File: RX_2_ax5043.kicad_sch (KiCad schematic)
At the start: 19 parts, among them P2 CONUFL001-SMD-T, Q4 DMP2160UWQ-7, U15 AX5043

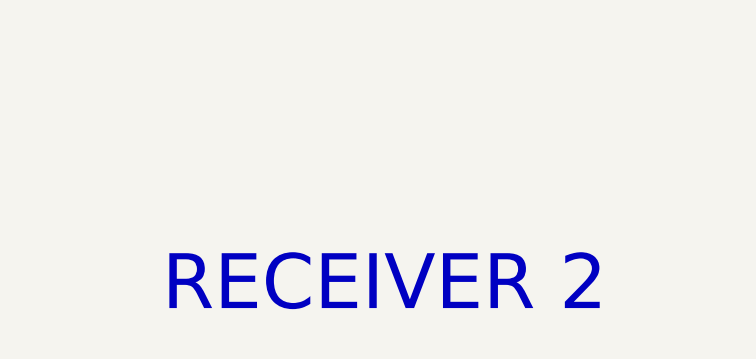
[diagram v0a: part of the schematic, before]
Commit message: Add licensing
Use CERN-OHL-W version 2

Signed-off-by: Corey Minyard <corey@minyard.net>
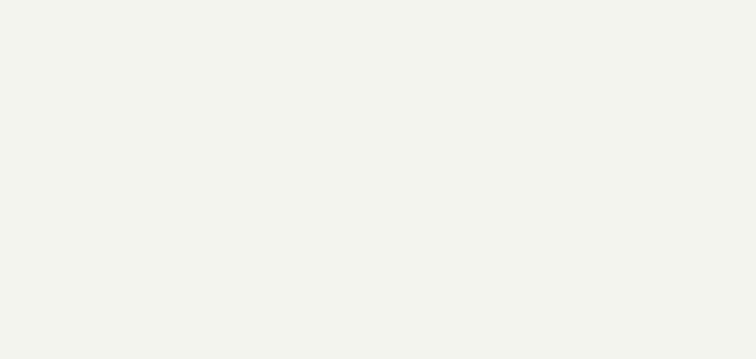
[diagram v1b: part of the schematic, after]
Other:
- note removed: "RECEIVER 2"
- title: Radiation Tolerant PacSat Communication -> AX5043 Receiver 1
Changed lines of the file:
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@@
 	(paper "USLedger")
 	(title_block
-		(title "Radiation Tolerant PacSat Communication")
-		(date "2023-06-17")
-		(rev "A")
+		(title "AX5043 Receiver 1")
+		(date "2026-08-20")
+		(rev "4.0")
 		(company "AMSAT-NA")
-		(comment 1 "N5BRG")
+		(comment 1 "AE5KM")
+		(comment 2 "Copyright Corey Minyard, 2026")
+		(comment 3 "Licensed under CERN-OHL-W version 2")
 	)
 	(text "Rx2+"
@@
 			)
 			(justify left bottom)
-		)
-	)
-	(text "RECEIVER 2"
-		(exclude_from_sim no)
-		(at 337.82 247.65 0)
-		(effects
-			(font
-				(size 6.096 6.096)
-			)
-			(justify left bottom)

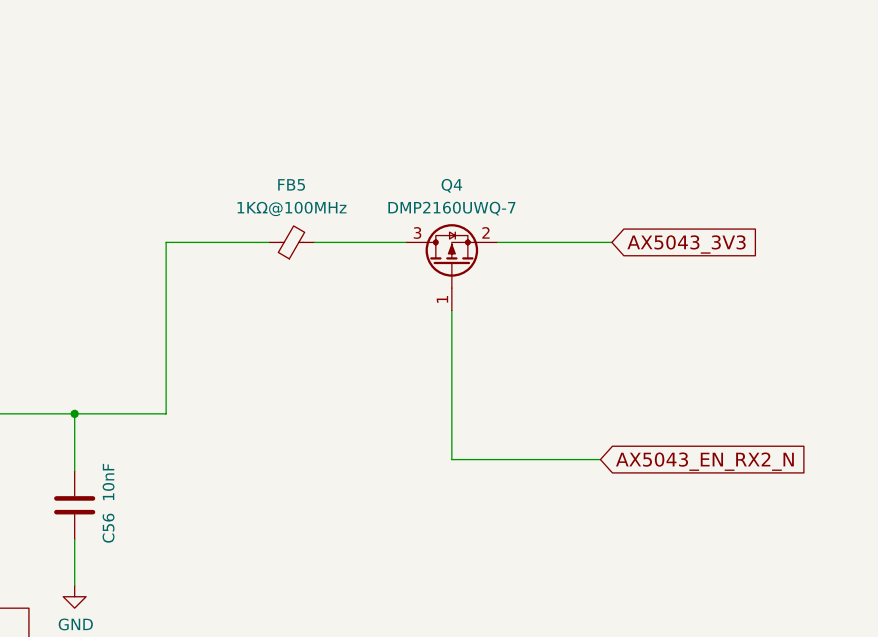
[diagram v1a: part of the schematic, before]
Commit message: Cost reduce the AX5043 power control
Change the MOSFET + ferrite bead combo on all the AX5043 power inputs
to a inrush-controlled power controller.  The space-rated ferrites are
just too expensive.

Signed-off-by: Corey Minyard <corey@minyard.net>
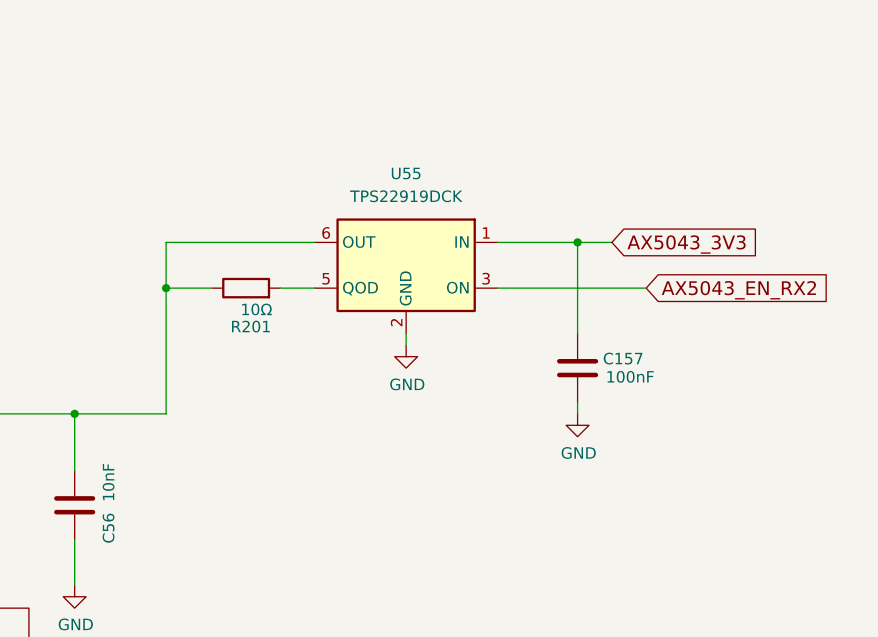
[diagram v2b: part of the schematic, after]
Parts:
- removed FB5: 1KΩ@100MHz, Inductor_SMD:L_0603_1608Metric_Pad1.05x0.95mm_HandSolder, symbol Device:FerriteBead_Small
- removed Q4: DMP2160UWQ-7, Package_TO_SOT_SMD:SOT-323_SC-70, symbol Transistor_FET:Q_PMOS_GSD
- added C157: 100nF, Capacitor_SMD:C_0402_1005Metric_Pad0.74x0.62mm_HandSolder, symbol Device:C
- added R201: 10Ω, Resistor_SMD:R_0402_1005Metric_Pad0.72x0.64mm_HandSolder, symbol Device:R
- added U55: TPS22919DCK, Package_TO_SOT_SMD:SOT-363_SC-70-6, symbol Power_Management:TPS22919DCK
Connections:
- net AX5043_3V3: now also C157.1, U55.1 (IN)
- net GND: now also C157.2, U55.2 (GND)
- net at C56.1, U15.23 (VDD_IO): now also R201.1, U55.6 (OUT)
- new net: R201.2, U55.5 (QOD)
- new net AX5043_EN_RX2: U55.3 (ON)

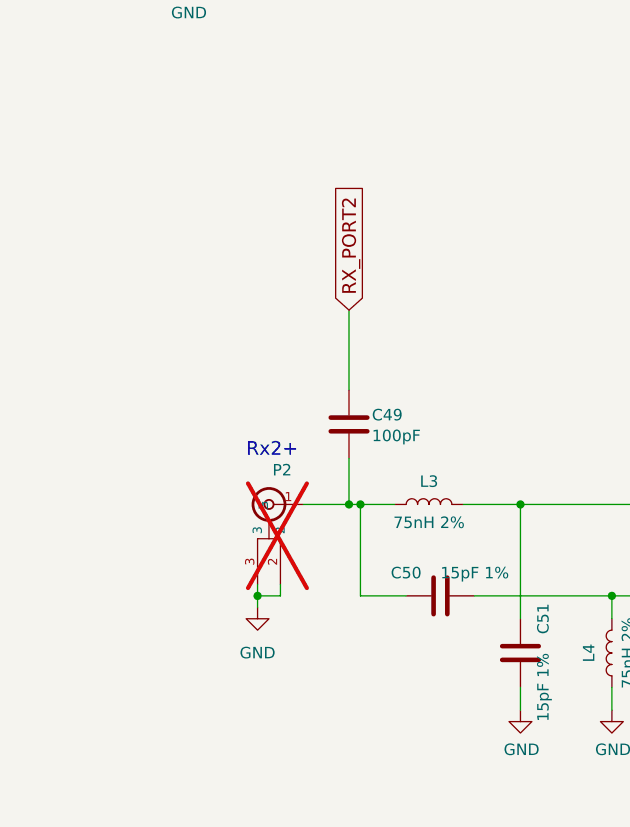
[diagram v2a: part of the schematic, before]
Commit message: Remove U.FL connectors from all AX5043 RX connections except AX5043 4
They aren't necessary.  If you need to pull off an RX line for another
board, you can use 4, and you can use 4 for testing.

Signed-off-by: Corey Minyard <corey@minyard.net>
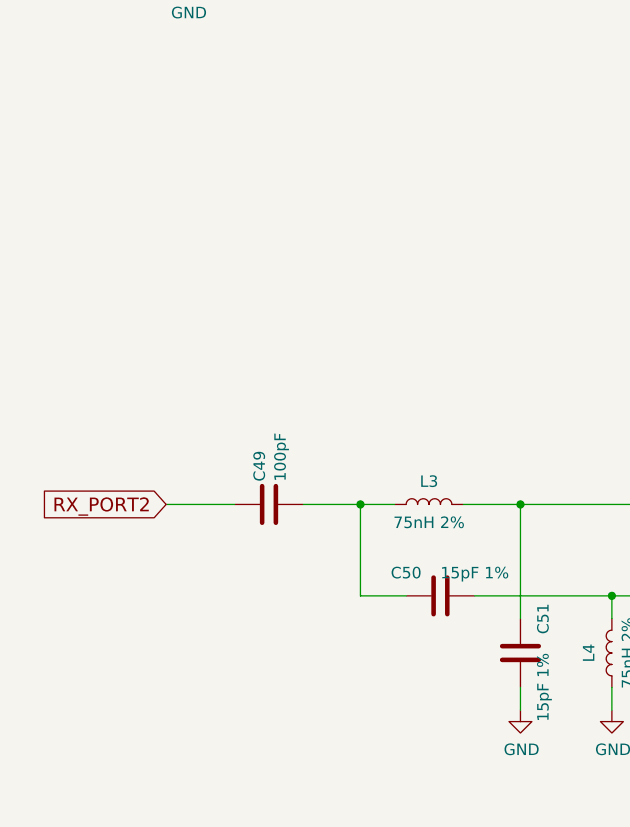
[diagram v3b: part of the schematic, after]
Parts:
- removed P2: CONUFL001-SMD-T, PacSatDev_misc:CONN1_CONUFL_TEC, symbol PACSAT_DEV_misc:U_FL
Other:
- note removed: "Rx2+"
- moved on the sheet: C49
